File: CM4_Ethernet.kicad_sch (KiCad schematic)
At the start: 6 parts

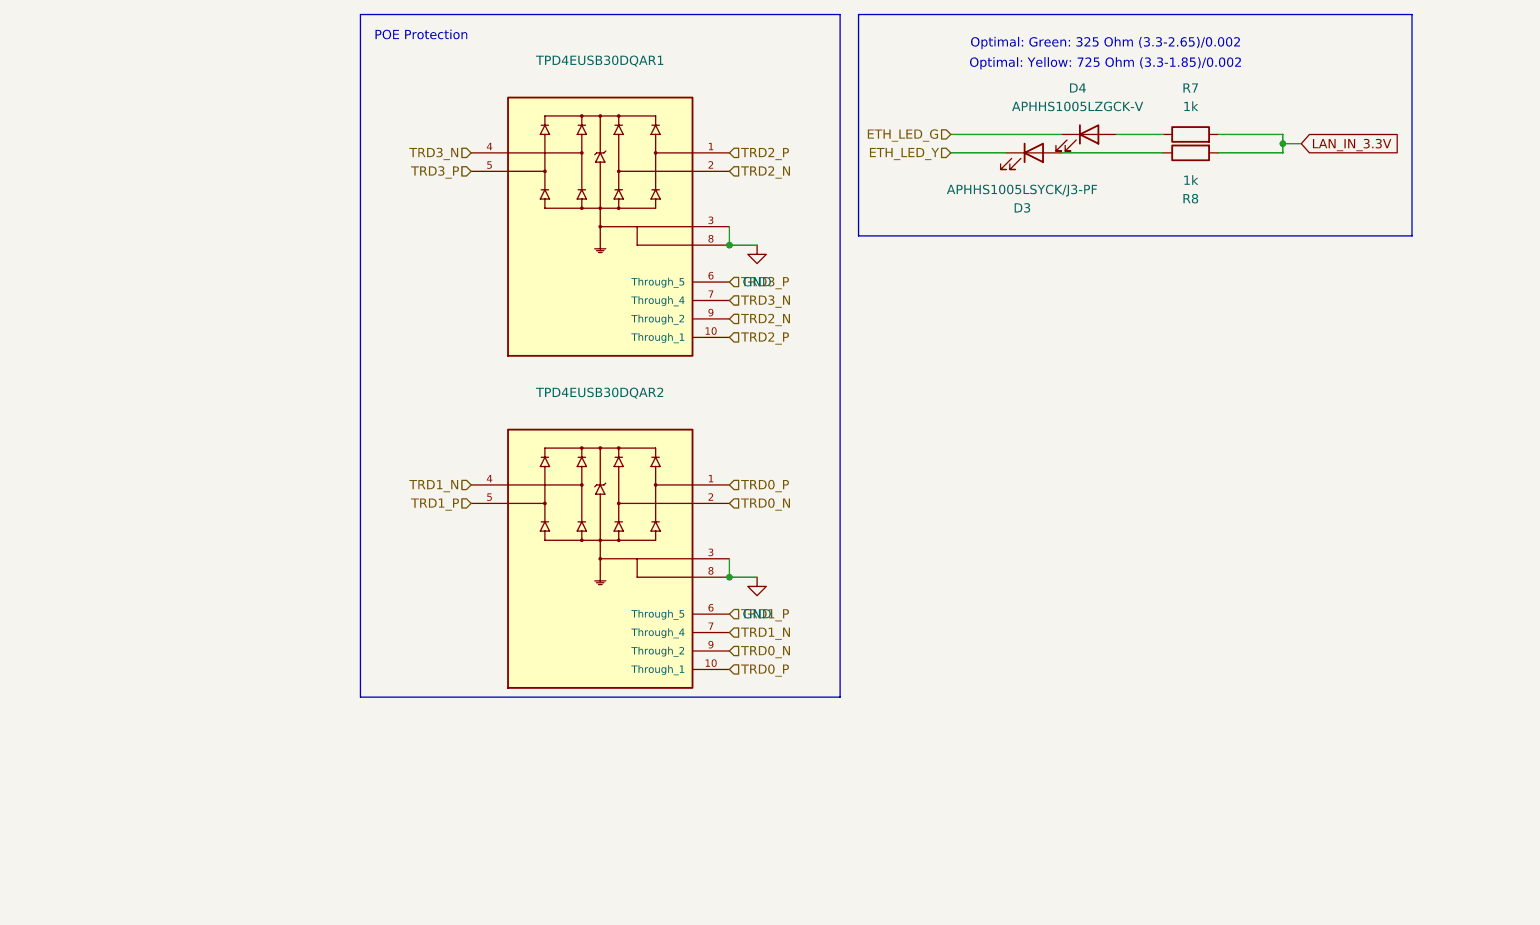
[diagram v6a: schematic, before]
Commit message: added lan bus
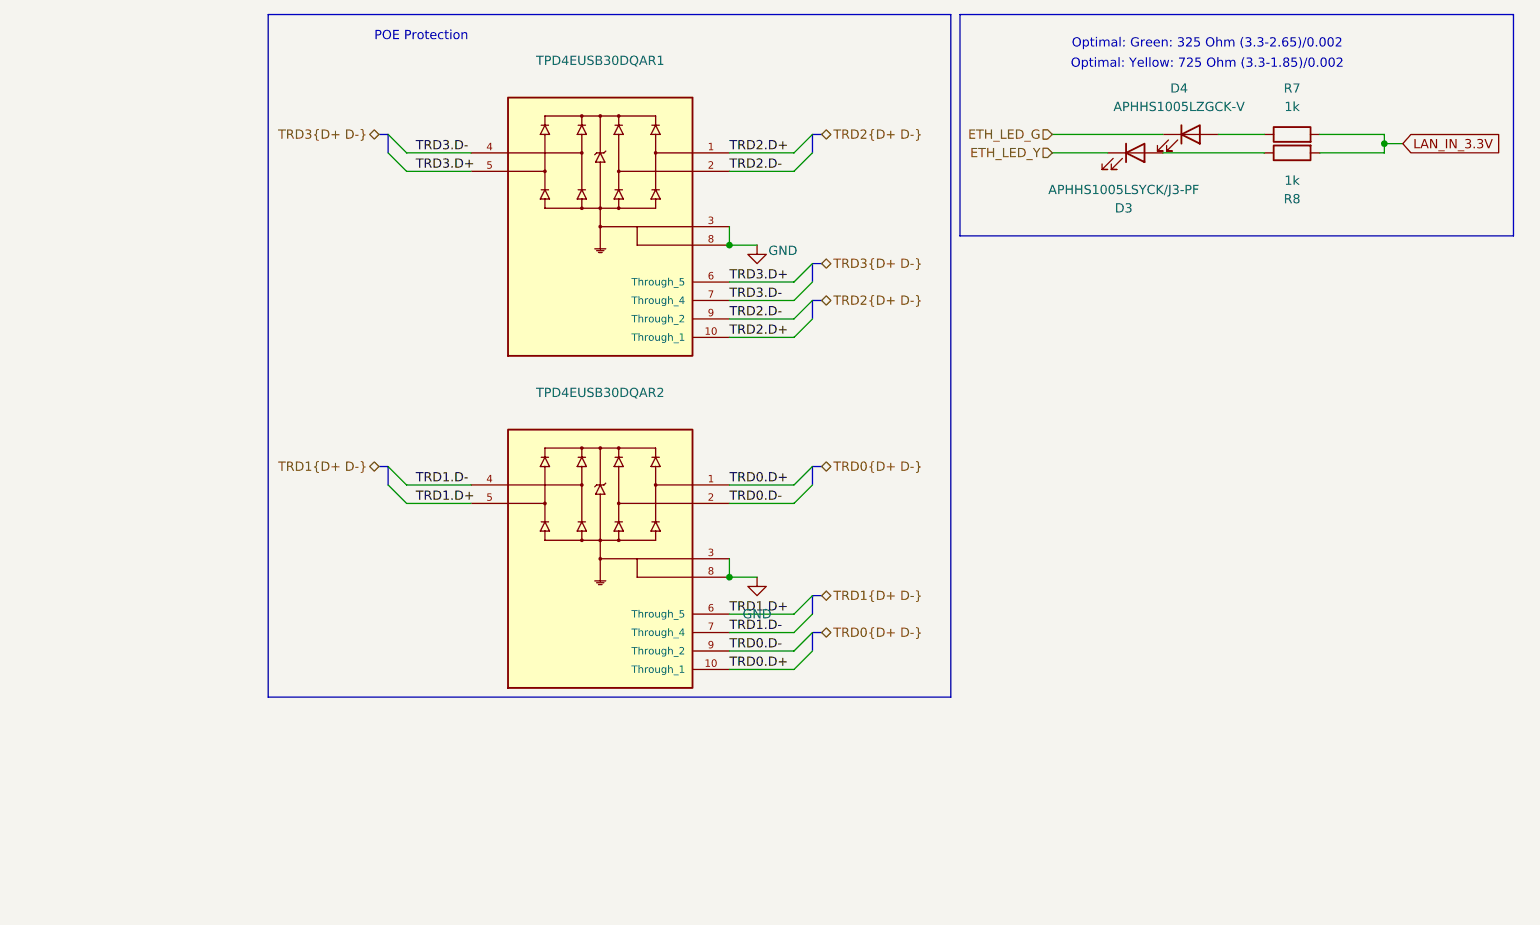
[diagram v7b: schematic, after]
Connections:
- net TRD0_N renamed TRD0.D-
- net TRD0_P renamed TRD0.D+
- net TRD1_N renamed TRD1.D-
- net TRD1_P renamed TRD1.D+
- net TRD2_N renamed TRD2.D-
- net TRD2_P renamed TRD2.D+
- net TRD3_N renamed TRD3.D-
- net TRD3_P renamed TRD3.D+
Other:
- moved on the sheet: D3, D4, R7, R8

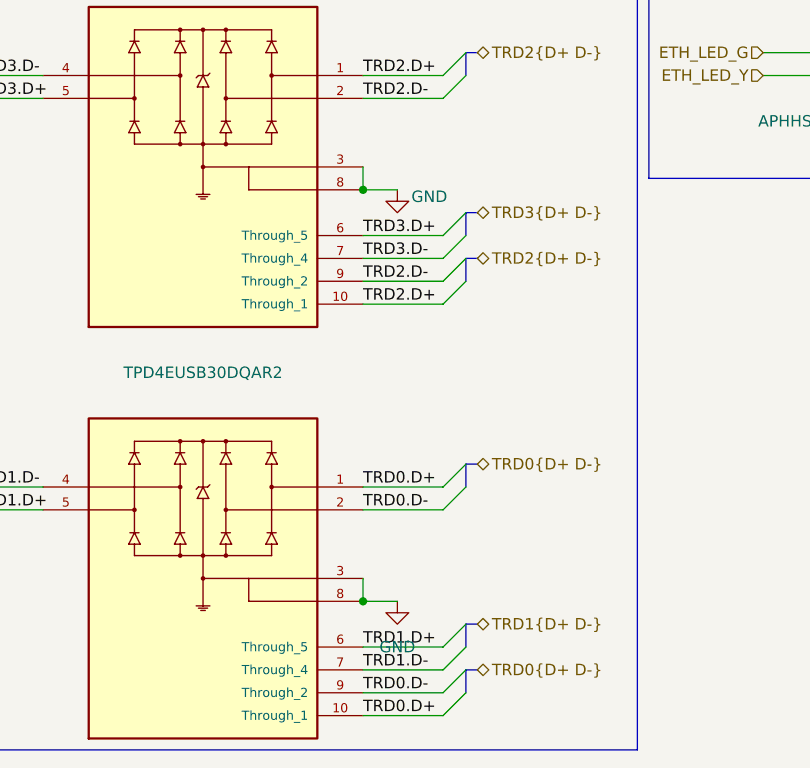
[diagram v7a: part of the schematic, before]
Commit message: chore: multiple cosmetic wiring changes
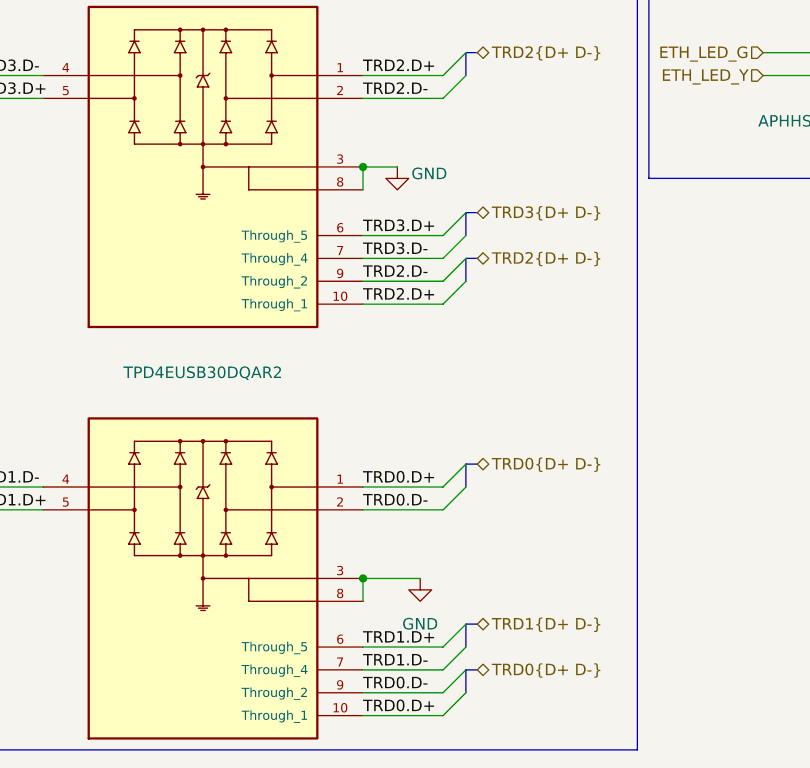
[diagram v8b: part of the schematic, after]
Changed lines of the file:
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@@
 	)
 	(junction
-		(at 134.62 57.15)
+		(at 134.62 54.61)
+		(diameter 0)
+		(color 0 0 0 0)
+	)
+	(junction
+		(at 134.62 100.33)
 		(diameter 0)
 		(color 0 0 0 0)
@@
 		(color 0 0 0 0)
 	)
-	(junction
-		(at 134.62 102.87)
-		(diameter 0)
-		(color 0 0 0 0)
-	)
 	(bus_entry
 		(at 146.05 44.45)
@@
 	(wire
 		(pts
-			(xy 134.62 57.15) (xy 138.43 57.15)
+			(xy 134.62 54.61) (xy 138.43 54.61)
 		)
 		(stroke
@@
 	(wire
 		(pts
-			(xy 134.62 102.87) (xy 138.43 102.87)
-		)
-		(stroke
-			(width 0)
-			(type default)
-		)
-	)
-	(wire
-		(pts
 			(xy 179.07 44.45) (xy 186.69 44.45)
 		)
@@
 		(pts
 			(xy 146.05 59.69) (xy 146.05 62.23)
+		)
+		(stroke
+			(width 0)
+			(type default)
+		)
+	)
+	(wire
+		(pts
+			(xy 134.62 100.33) (xy 140.97 100.33)
 		)
 		(stroke
@@
 	(symbol
 		(lib_id "power:GND")
-		(at 138.43 57.15 0)
+		(at 138.43 54.61 0)
 		(unit 1)
 		(exclude_from_sim no)
@@
 		(dnp no)
 		(property "Reference" "#PWR019"
-			(at 138.43 63.5 0)
+			(at 138.43 60.96 0)
 			(effects
 				(font
@@
 		)
 		(property "Value" "GND"
-			(at 141.986 57.912 0)
+			(at 141.986 55.372 0)
 			(effects
 				(font
@@
 		)
 		(property "Footprint" ""
-			(at 138.43 57.15 0)
+			(at 138.43 54.61 0)
 			(effects
 				(font
@@
 		)
 		(property "Datasheet" ""
-			(at 138.43 57.15 0)
+			(at 138.43 54.61 0)
 			(effects
 				(font
@@
 		)
 		(property "Description" "Power symbol creates a global label with name \"GND\" , ground"
-			(at 138.43 57.15 0)
+			(at 138.43 54.61 0)
 			(effects
 				(font
@@
 	(symbol
 		(lib_id "power:GND")
-		(at 138.43 102.87 0)
+		(at 140.97 100.33 0)
 		(unit 1)
 		(exclude_from_sim no)
@@
 		(fields_autoplaced yes)
 		(property "Reference" "#PWR020"
-			(at 138.43 109.22 0)
+			(at 140.97 106.68 0)
 			(effects
 				(font
@@
 		)
 		(property "Value" "GND"
-			(at 138.43 107.95 0)
+			(at 140.97 105.41 0)
 			(effects
 				(font
@@
 		)
 		(property "Footprint" ""
-			(at 138.43 102.87 0)
+			(at 140.97 100.33 0)
 			(effects
 				(font
@@
 		)
 		(property "Datasheet" ""
-			(at 138.43 102.87 0)
+			(at 140.97 100.33 0)
 			(effects
 				(font
@@
 		)
 		(property "Description" "Power symbol creates a global label with name \"GND\" , ground"
-			(at 138.43 102.87 0)
-			(effects
-				(font
+			(at 140.97 100.33 0)
+			(effects
+				(font
